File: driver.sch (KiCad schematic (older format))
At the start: 32 parts, among them Q1 Q_NMOS_GDSD, Q10 Q_NMOS_GDSD, Q11 Q_NMOS_GDSD, Q12 Q_NMOS_GDSD, Q13 Q_NMOS_GDSD, Q14 Q_NMOS_GDSD, Q15 Q_NMOS_GDSD, Q16 Q_NMOS_GDSD, Q2 Q_NMOS_GDSD, Q3 Q_NMOS_GDSD, Q4 Q_NMOS_GDSD, Q5 Q_NMOS_GDSD, Q6 Q_NMOS_GDSD, Q7 Q_NMOS_GDSD, Q8 Q_NMOS_GDSD, Q9 Q_NMOS_GDSD, U1 PCA9685PW

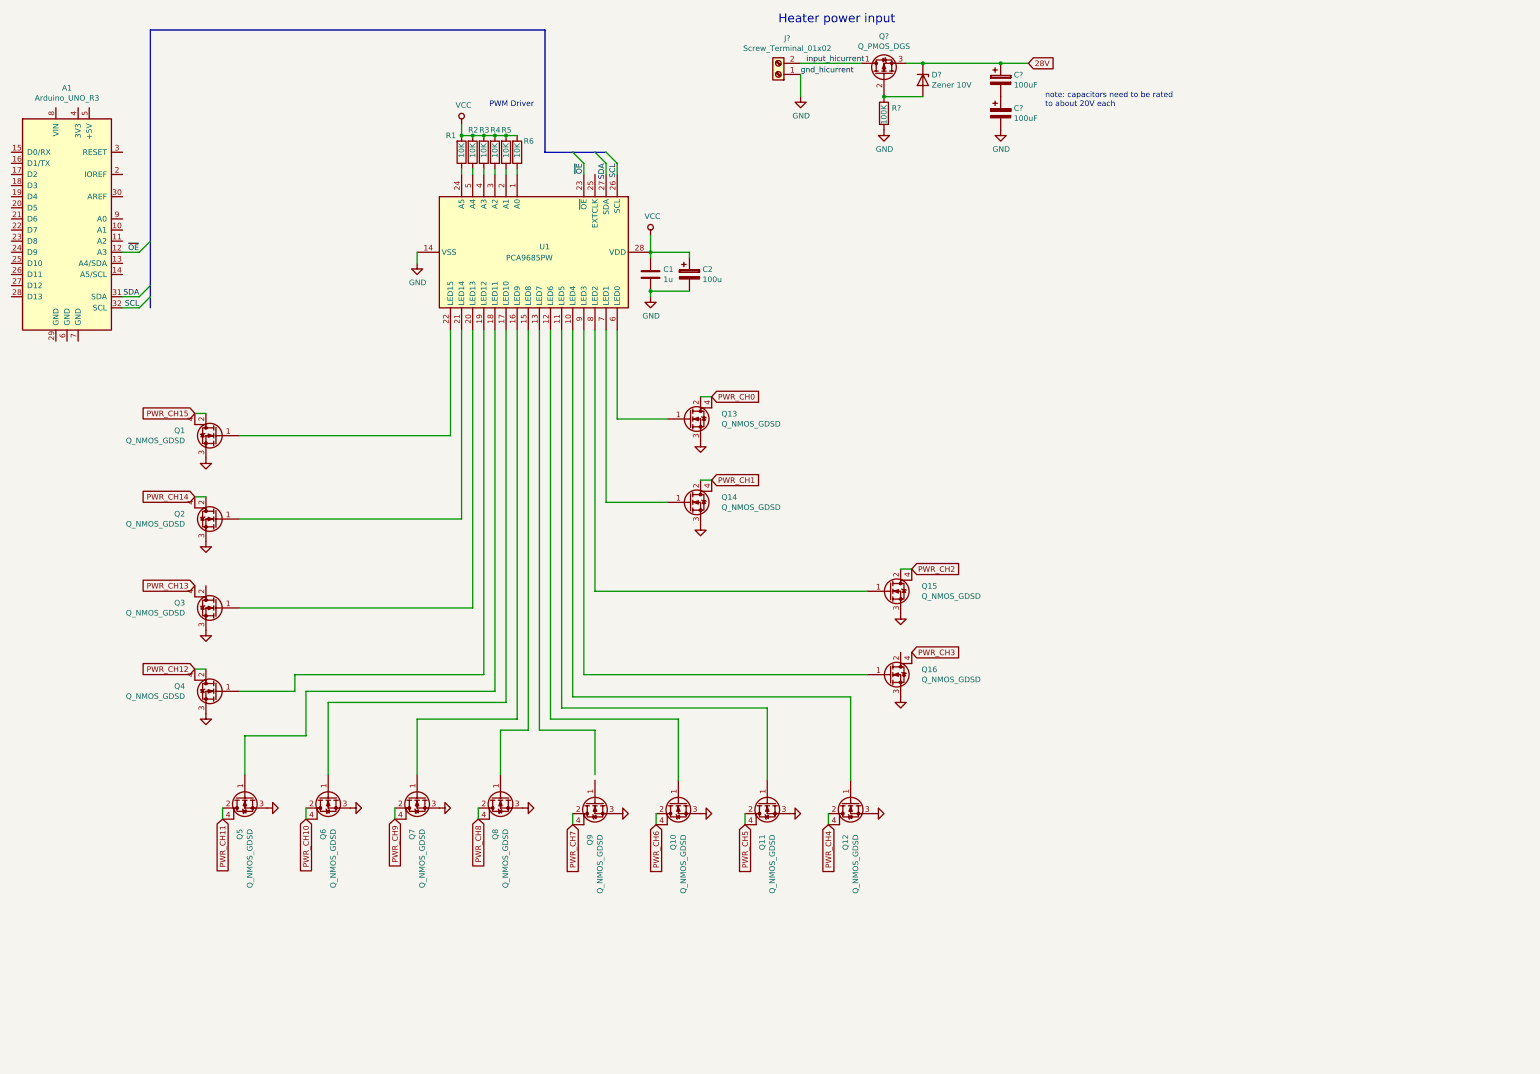
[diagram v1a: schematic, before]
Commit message: connector selected, beginning routing
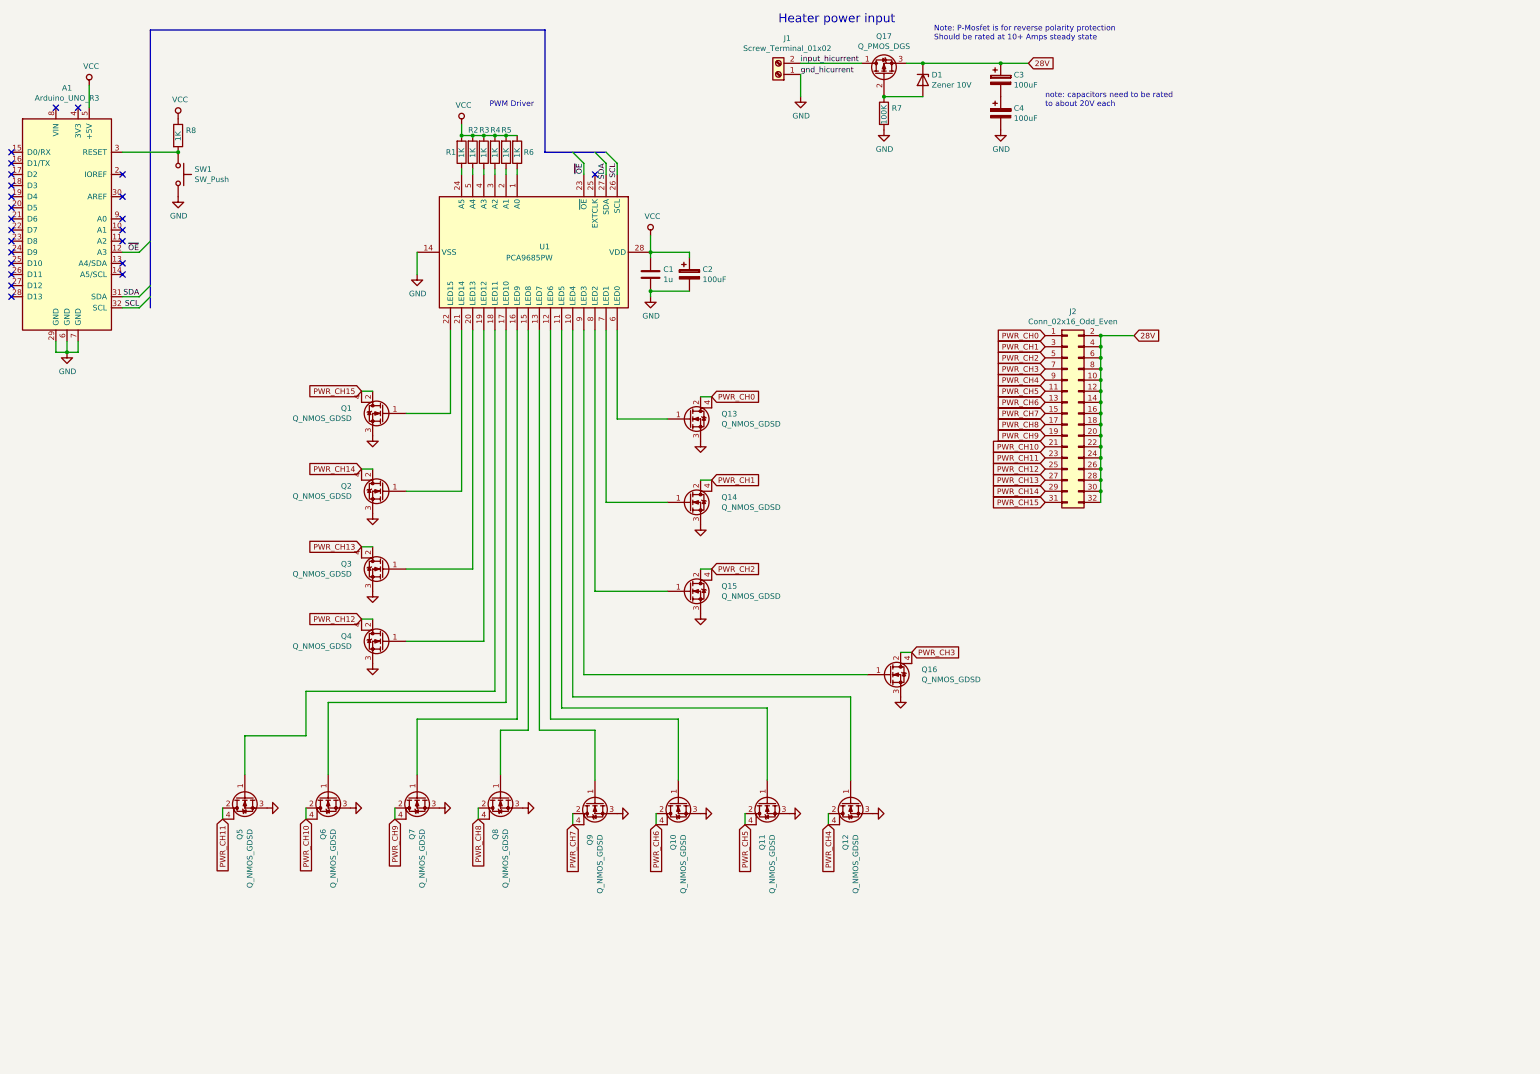
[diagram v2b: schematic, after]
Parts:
- added J2: Conn_02x16_Odd_Even, Connector_PinHeader_2.54mm:PinHeader_2x16_P2.54mm_Vertical, symbol Connector_Generic:Conn_02x16_Odd_Even
- added R8: 1K, Resistor_SMD:R_0805_2012Metric_Pad1.15x1.40mm_HandSolder, symbol Device:R
- added SW1: SW_Push, Button_Switch_SMD:SW_SPST_B3S-1000, symbol Switch:SW_Push
- C2: value 100u -> 100uF
- C3, C4: renamed from C?; footprint (none) -> Capacitor_THT:CP_Radial_D8.0mm_P3.50mm
- D1: renamed from D?; footprint (none) -> Diode_SMD:D_1206_3216Metric_Pad1.42x1.75mm_HandSolder
- J1: renamed from J?; footprint (none) -> TerminalBlock_MetzConnect:TerminalBlock_MetzConnect_Type055_RT01502HDWU_1x02_P5.00mm_Horizontal
- Q17: renamed from Q?; footprint (none) -> Package_TO_SOT_SMD:TO-252-2
- R1, R2, R3, R4, R5, R6: value 10K -> 1K
- R7: renamed from R?; footprint (none) -> Resistor_SMD:R_0805_2012Metric_Pad1.15x1.40mm_HandSolder
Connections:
- net 28V: now also J2.10 (Pin_10), J2.12 (Pin_12), J2.14 (Pin_14), J2.16 (Pin_16), J2.18 (Pin_18), J2.2 (Pin_2), J2.20 (Pin_20), J2.22 (Pin_22), J2.24 (Pin_24), J2.26 (Pin_26), J2.28 (Pin_28), J2.30 (Pin_30), J2.32 (Pin_32), J2.4 (Pin_4), J2.6 (Pin_6), J2.8 (Pin_8)
- net GND: now also A1.29 (GND), A1.6 (GND), A1.7 (GND), SW1.2
- net PWR_CH0: now also J2.1 (Pin_1)
- net PWR_CH1: now also J2.3 (Pin_3)
- net PWR_CH10: now also J2.21 (Pin_21)
- net PWR_CH11: now also J2.23 (Pin_23)
- net PWR_CH12: now also J2.25 (Pin_25)
- net PWR_CH13: now also Q3.2 (D), J2.27 (Pin_27)
- net PWR_CH14: now also J2.29 (Pin_29)
- net PWR_CH15: now also J2.31 (Pin_31)
- net PWR_CH2: now also J2.5 (Pin_5)
- net PWR_CH3: now also Q16.2 (D), J2.7 (Pin_7)
- net PWR_CH4: now also J2.9 (Pin_9)
- net PWR_CH5: now also J2.11 (Pin_11)
- net PWR_CH6: now also J2.13 (Pin_13)
- net PWR_CH7: now also J2.15 (Pin_15)
- net PWR_CH8: now also J2.17 (Pin_17)
- net PWR_CH9: now also J2.19 (Pin_19)
- net VCC: now also A1.5 (+5V), R8.1
- net at A1.3 (RESET): now also R8.2, SW1.1
- net at U1.13 (LED7): now also Q9.1 (G)
- no-connect marks 0 -> 24
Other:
- note added: "Note: P-Mosfet is for reverse polarity protection\nShould be rated at 10+ Amps steady state"
- moved on the sheet: Q1, Q15, Q2, Q3, Q4

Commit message: reroute schematic + component placement
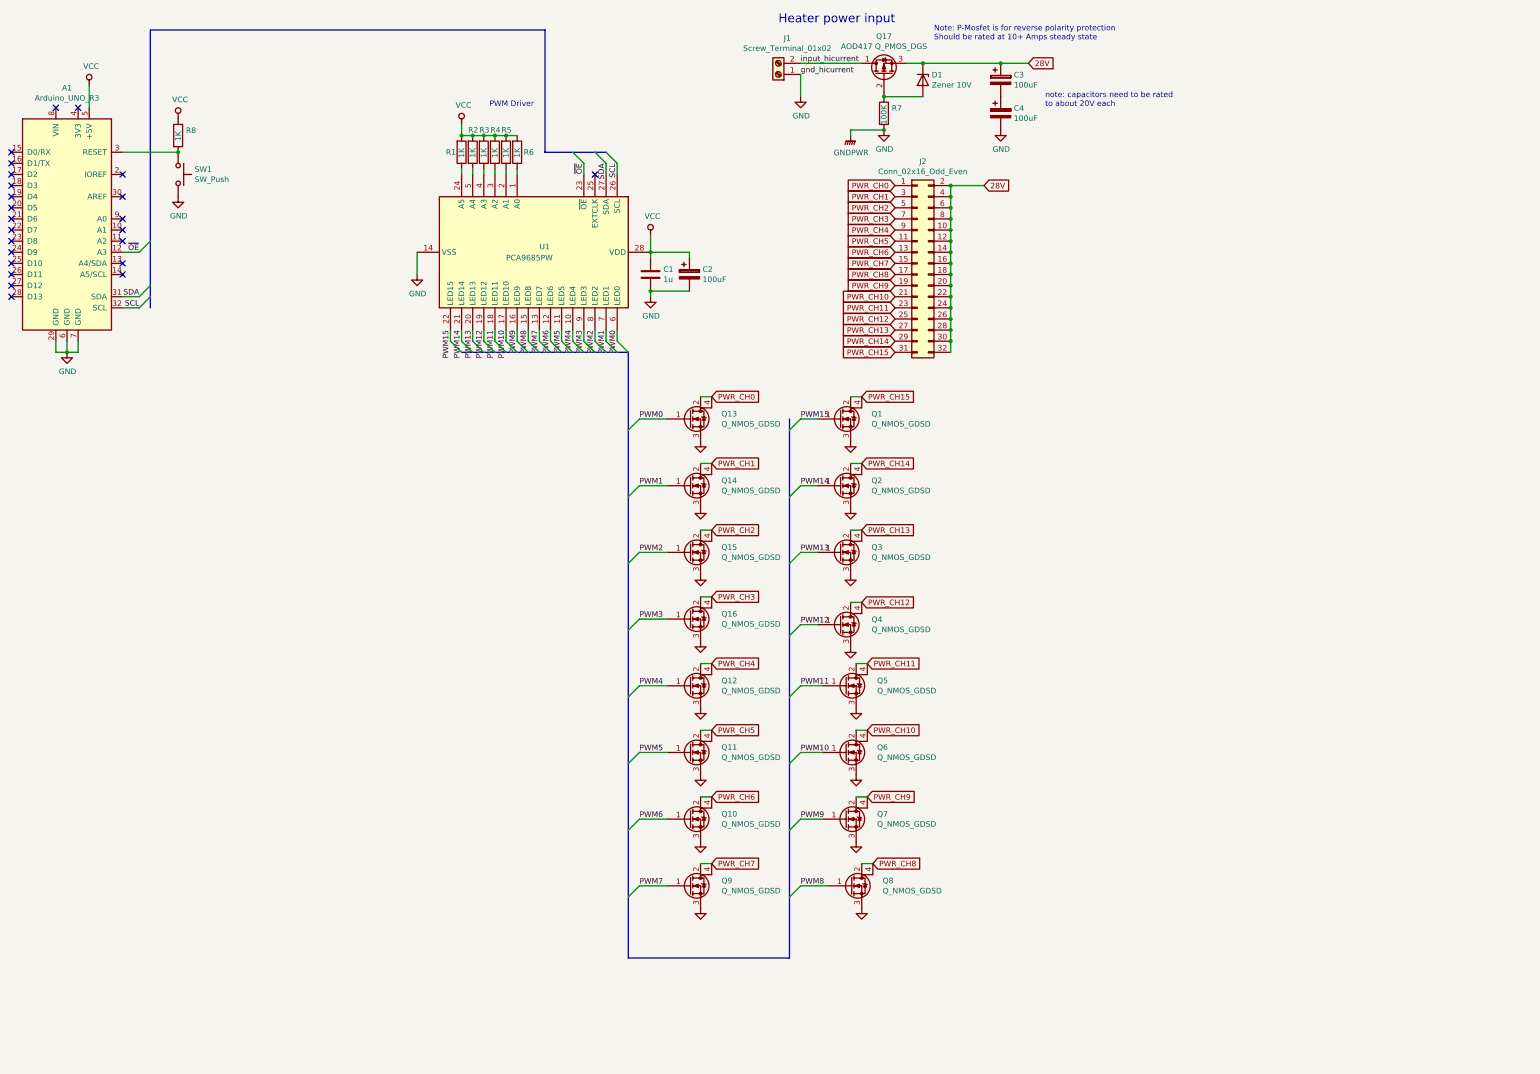
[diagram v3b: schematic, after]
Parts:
- Q17: value Q_PMOS_DGS -> AOD417 Q_PMOS_DGS
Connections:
- net PWM4: now reaches Q12.1 (G), U1.10 (LED4)
- net PWM5: now reaches Q11.1 (G), U1.11 (LED5)
- net PWM6: now reaches Q10.1 (G), U1.12 (LED6)
- net PWM7: now reaches Q9.1 (G), U1.13 (LED7)
- net PWM8: now reaches Q8.1 (G), U1.15 (LED8)
- net PWM9: now reaches Q7.1 (G), U1.16 (LED9)
- net PWM10: now reaches Q6.1 (G), U1.17 (LED10)
- net PWM11: now reaches Q5.1 (G), U1.18 (LED11)
- net PWM12: now reaches Q4.1 (G), U1.19 (LED12)
- net PWM13: now reaches Q3.1 (G), U1.20 (LED13)
- net PWM14: now reaches Q2.1 (G), U1.21 (LED14)
- net PWM15: now reaches Q1.1 (G), U1.22 (LED15)
- net PWM0: now reaches Q13.1 (G), U1.6 (LED0)
- net PWM1: now reaches Q14.1 (G), U1.7 (LED1)
- net PWM2: now reaches Q15.1 (G), U1.8 (LED2)
- net PWM3: now reaches Q16.1 (G), U1.9 (LED3)
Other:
- moved on the sheet: J2, Q1, Q10, Q11, Q12, Q14, Q15, Q16, Q2, Q3, Q4, Q5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

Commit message: Trudy's notes
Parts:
- removed C3, C4: 100uF, Capacitor_THT:CP_Radial_D8.0mm_P3.50mm, symbol Device:CP
- added C?: CP, symbol Device:CP
- added C?: C, symbol Device:C
- added R? (x2): 10k, symbol Device:R
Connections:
- net 28V: now also C?.1, C?.1
- net GND: now also C?.2, C?.2
- net SCL: now also R?.2
- net SDA: now also R?.2
- net VCC: now also R?.1, R?.1
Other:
- note added: "100mA in each MOSFET"
- note added: "Add pull up and down resistors\ncheck whether chip can source or sink properly"
- note added: "Connector to heaters is just a pin header.\nRated at 1 A per contact"
- note added: "Heater Driver PCB"
- note added: "I2C"
- note added: "P-Mosfet is for reverse polarity protection\nShould be rated at 10+ Amps steady state.\nExpect 6 A."
- note added: "PWM channels"
- note added: "Reset"
- note added: "change footprint of big caps"
- note added: "check extclk. No connect ok?"
- note removed: "Note: P-Mosfet is for reverse polarity protection\nShould be rated at 10+ Amps steady state"
- note removed: "note: capacitors need to be rated\nto about 20V each"
- moved on the sheet: J2

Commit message: add pulldown resistors
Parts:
- removed R2, R3, R4, R5, R6: 1K, Resistor_SMD:R_0805_2012Metric_Pad1.15x1.40mm_HandSolder, symbol Device:R
- added R10, R11, R12, R13, R14, R15, R16, R17, R18, R19, R20, R21, R4, R5, R6, R9: 10k, Resistor_SMD:R_0805_2012Metric_Pad1.15x1.40mm_HandSolder, symbol Device:R_Small
- R2, R3: renamed from R?; footprint (none) -> Resistor_SMD:R_0805_2012Metric_Pad1.15x1.40mm_HandSolder
- R7: value 100K -> 10K
- gave numbers to parts that had none: 2
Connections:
- net GND: now also R10.2, R11.2, R12.2, R13.2, R14.2, R15.2, R16.2, R17.2, R18.2, R19.2, R20.2, R21.2, R4.2, R5.2, R6.2, R9.2
- net PWM0: now also R4.1
- net PWM1: now also R5.1
- net PWM10: now also R19.1
- net PWM11: now also R18.1
- net PWM12: now also R17.1
- net PWM13: now also R16.1
- net PWM14: now also R15.1
- net PWM15: now also R14.1
- net PWM2: now also R6.1
- net PWM3: now also R9.1
- net PWM4: now also R10.1
- net PWM5: now also R11.1
- net PWM6: now also R12.1
- net PWM7: now also R13.1
- net PWM8: now also R21.1
- net PWM9: now also R20.1
- net at U1.1 (A0): now also R1.1, U1.2 (A1), U1.24 (A5), U1.3 (A2), U1.4 (A3), U1.5 (A4)
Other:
- note added: "Reset (optional)"
- note removed: "Reset"

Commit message: ground extclk as per datasheet
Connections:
- net GND: now also U1.25 (EXTCLK)
- no-connect marks 24 -> 23
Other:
- note removed: "check extclk. No connect ok?"
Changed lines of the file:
@@
 Wire Wire Line
 	8700 5550 8600 5550
-NoConn ~ 6300 2350
 $Comp
 L power:VCC #PWR018
@@
 	6500 1400 6500 1550
 Connection ~ 6450 1400
-Text Notes 6650 2400 0    157  ~ 0
-check extclk. No connect ok?
 Text Notes 7000 4000 0    157  ~ 0
 Add pull up and down resistors\ncheck whether chip can source or sink properly
 Text Notes 10500 1700 0    157  ~ 0
 change footprint of big caps
-Wire Wire Line
-	6500 1850 6500 2350
 Wire Wire Line
 	5100 2300 5200 2300
@@
 Wire Wire Line
 	6900 6400 6900 6350
+Connection ~ 6900 6350
+Wire Wire Line
+	6900 6350 6950 6350
+Wire Wire Line
+	6500 1850 6500 2350
+$Comp
+L power:GND #PWR?
+U 1 1 5C4D7BC3
+P 6300 2300
+F 0 "#PWR?" H 6300 2050 50  0001 C CNN
+F 1 "GND" V 6350 2300 50  0000 C CNN
+F 2 "" H 6300 2300 50  0001 C CNN
+F 3 "" H 6300 2300 50  0001 C CNN
+	1    6300 2300
+	-1   0    0    1
+$EndComp
+Wire Wire Line
+	6300 2300 6300 2350
 Wire Wire Line
 	6400 1850 6400 2350
@@
 Wire Bus Line
 	8050 4550 8050 9400
-Connection ~ 6900 6350
-Wire Wire Line
-	6900 6350 6950 6350
 $EndSCHEMATC

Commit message: change address
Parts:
- added R22, R23, R24, R25, R26: 1K, Resistor_SMD:R_0805_2012Metric_Pad1.15x1.40mm_HandSolder, symbol Device:R
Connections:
- net GND: now also R1.2, R23.2, R25.2
- net VCC: now also R22.2, R24.2, R26.2; no longer R1.2
- new net: R26.1, U1.1 (A0)
- new net: R25.1, U1.2 (A1)
- new net: R1.1, U1.24 (A5)
- new net: R24.1, U1.3 (A2)
- new net: R23.1, U1.4 (A3)
- new net: R22.1, U1.5 (A4)
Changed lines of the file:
@@
 L power:VCC #PWR0107
 U 1 1 5C1B585A
-P 5100 1900
-F 0 "#PWR0107" H 5100 1750 50  0001 C CNN
-F 1 "VCC" H 5117 2073 50  0000 C CNN
-F 2 "" H 5100 1900 50  0001 C CNN
-F 3 "" H 5100 1900 50  0001 C CNN
-	1    5100 1900
+P 5200 1900
+F 0 "#PWR0107" H 5200 1750 50  0001 C CNN
+F 1 "VCC" H 5217 2073 50  0000 C CNN
+F 2 "" H 5200 1900 50  0001 C CNN
+F 3 "" H 5200 1900 50  0001 C CNN
+	1    5200 1900
 	1    0    0    -1
 $EndComp
 Wire Wire Line
 	5100 2300 5100 2350
-Wire Wire Line
-	5200 2300 5200 2350
-Wire Wire Line
-	5300 2300 5300 2350
-Wire Wire Line
-	5400 2300 5400 2350
-Wire Wire Line
-	5500 2300 5500 2350
-Wire Wire Line
-	5600 2300 5600 2350
-Wire Wire Line
-	5100 1900 5100 2000
 $Comp
 L Device:R R1
@@
 Text Notes 10500 1700 0    157  ~ 0
 change footprint of big caps
-Wire Wire Line
-	5100 2300 5200 2300
-Connection ~ 5100 2300
-Wire Wire Line
-	5200 2300 5300 2300
-Connection ~ 5200 2300
-Connection ~ 5300 2300
-Wire Wire Line
-	5300 2300 5400 2300
-Connection ~ 5400 2300
-Wire Wire Line
-	5400 2300 5500 2300
-Wire Wire Line
-	5600 2300 5500 2300
-Connection ~ 5500 2300
 $Comp
 L Device:R_Small R4
@@
 	6500 1850 6500 2350
 $Comp
-L power:GND #PWR?
+L power:GND #PWR0106
 U 1 1 5C4D7BC3
 P 6300 2300
-F 0 "#PWR?" H 6300 2050 50  0001 C CNN
+F 0 "#PWR0106" H 6300 2050 50  0001 C CNN
 F 1 "GND" V 6350 2300 50  0000 C CNN
 F 2 "" H 6300 2300 50  0001 C CNN
@@
 Wire Wire Line
 	6300 2300 6300 2350
+$Comp
+L Device:R R23
+U 1 1 5C4E9154
+P 5300 2150
+F 0 "R23" H 5250 2150 50  0000 R CNN
+F 1 "1K" V 5300 2200 50  0000 R CNN
+F 2 "Resistor_SMD:R_0805_2012Metric_Pad1.15x1.40mm_HandSolder" V 5230 2150 50  0001 C CNN
+F 3 "~" H 5300 2150 50  0001 C CNN
+	1    5300 2150
+	1    0    0    1
+$EndComp
+$Comp
+L Device:R R24
+U 1 1 5C4E91D2
+P 5400 2150
+F 0 "R24" H 5350 2150 50  0000 R CNN
+F 1 "1K" V 5400 2200 50  0000 R CNN
+F 2 "Resistor_SMD:R_0805_2012Metric_Pad1.15x1.40mm_HandSolder" V 5330 2150 50  0001 C CNN
+F 3 "~" H 5400 2150 50  0001 C CNN
+	1    5400 2150
+	1    0    0    1
+$EndComp
+$Comp
+L Device:R R22
+U 1 1 5C4E92AE
+P 5200 2150
+F 0 "R22" H 5150 2150 50  0000 R CNN
+F 1 "1K" V 5200 2200 50  0000 R CNN
+F 2 "Resistor_SMD:R_0805_2012Metric_Pad1.15x1.40mm_HandSolder" V 5130 2150 50  0001 C CNN
+F 3 "~" H 5200 2150 50  0001 C CNN
+	1    5200 2150
+	1    0    0    1
+$EndComp
+$Comp
+L Device:R R25
+U 1 1 5C4E9324
+P 5500 2150
+F 0 "R25" H 5450 2150 50  0000 R CNN
+F 1 "1K" V 5500 2200 50  0000 R CNN
+F 2 "Resistor_SMD:R_0805_2012Metric_Pad1.15x1.40mm_HandSolder" V 5430 2150 50  0001 C CNN
+F 3 "~" H 5500 2150 50  0001 C CNN
+	1    5500 2150
+	1    0    0    1
+$EndComp
+$Comp
+L Device:R R26
+U 1 1 5C4E939C
+P 5600 2150
+F 0 "R26" H 5550 2150 50  0000 R CNN
+F 1 "1K" V 5600 2200 50  0000 R CNN
+F 2 "Resistor_SMD:R_0805_2012Metric_Pad1.15x1.40mm_HandSolder" V 5530 2150 50  0001 C CNN
+F 3 "~" H 5600 2150 50  0001 C CNN
+	1    5600 2150
+	1    0    0    1
+$EndComp
+$Comp
+L power:VCC #PWR0109
+U 1 1 5C4E94F8
+P 5400 1900
+F 0 "#PWR0109" H 5400 1750 50  0001 C CNN
+F 1 "VCC" H 5417 2073 50  0000 C CNN
+F 2 "" H 5400 1900 50  0001 C CNN
+F 3 "" H 5400 1900 50  0001 C CNN
+	1    5400 1900
+	1    0    0    -1
+$EndComp
+$Comp
+L power:VCC #PWR0110
+U 1 1 5C4E956D
+P 5600 1900
+F 0 "#PWR0110" H 5600 1750 50  0001 C CNN
+F 1 "VCC" H 5617 2073 50  0000 C CNN
+F 2 "" H 5600 1900 50  0001 C CNN
+F 3 "" H 5600 1900 50  0001 C CNN
+	1    5600 1900
+	1    0    0    -1
+$EndComp
+$Comp
+L power:GND #PWR0111
+U 1 1 5C4E95E2
+P 5100 1900
+F 0 "#PWR0111" H 5100 1650 50  0001 C CNN
+F 1 "GND" V 5150 1900 50  0000 C CNN
+F 2 "" H 5100 1900 50  0001 C CNN
+F 3 "" H 5100 1900 50  0001 C CNN
+	1    5100 1900
+	-1   0    0    1
+$EndComp
+$Comp
+L power:GND #PWR0112
+U 1 1 5C4E9657
+P 5300 1900
+F 0 "#PWR0112" H 5300 1650 50  0001 C CNN
+F 1 "GND" V 5350 1900 50  0000 C CNN
+F 2 "" H 5300 1900 50  0001 C CNN
+F 3 "" H 5300 1900 50  0001 C CNN
+	1    5300 1900
+	-1   0    0    1
+$EndComp
+$Comp
+L power:GND #PWR0113
+U 1 1 5C4E96CC
+P 5500 1900
+F 0 "#PWR0113" H 5500 1650 50  0001 C CNN
+F 1 "GND" V 5550 1900 50  0000 C CNN
+F 2 "" H 5500 1900 50  0001 C CNN
+F 3 "" H 5500 1900 50  0001 C CNN
+	1    5500 1900
+	-1   0    0    1
+$EndComp
+Wire Wire Line
+	5100 1900 5100 2000
+Wire Wire Line
+	5200 1900 5200 2000
+Wire Wire Line
+	5300 1900 5300 2000
+Wire Wire Line
+	5400 1900 5400 2000
+Wire Wire Line
+	5500 1900 5500 2000
+Wire Wire Line
+	5600 1900 5600 2000
+Wire Wire Line
+	5200 2300 5200 2350
+Wire Wire Line
+	5300 2300 5300 2350
+Wire Wire Line
+	5400 2300 5400 2350
+Wire Wire Line
+	5500 2300 5500 2350
+Wire Wire Line
+	5600 2300 5600 2350
 Wire Wire Line
 	6400 1850 6400 2350
